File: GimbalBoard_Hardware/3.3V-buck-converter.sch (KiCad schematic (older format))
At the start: 3 parts

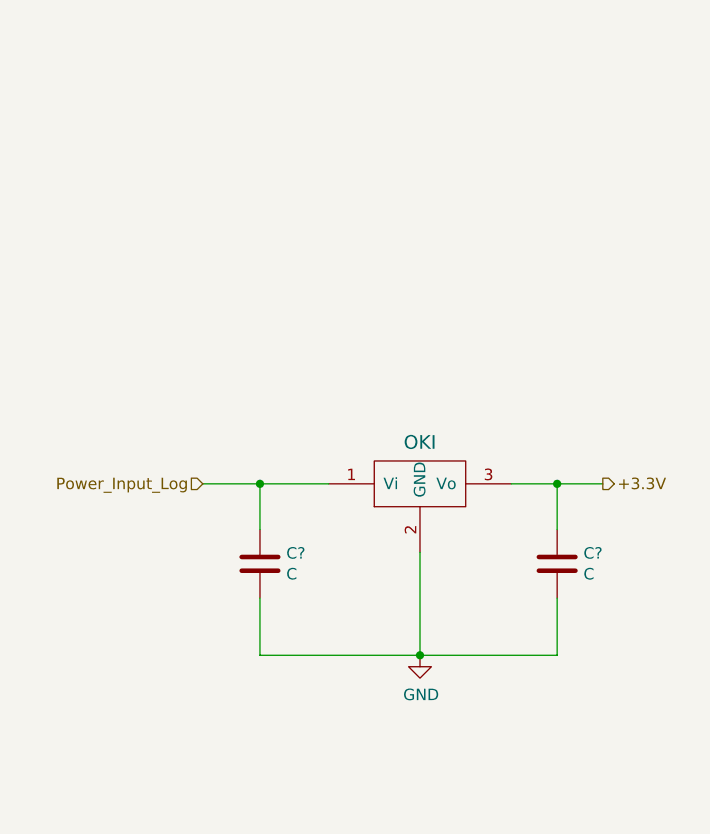
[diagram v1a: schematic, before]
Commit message: connected everything up and changed power to accomodate teensy instead of tiva
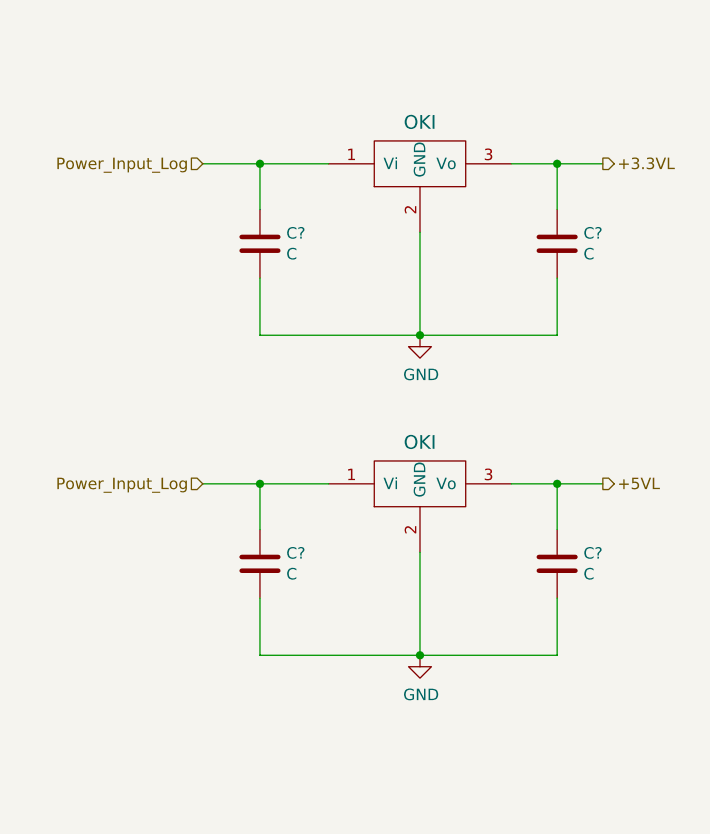
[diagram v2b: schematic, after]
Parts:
- added C? (x2): C, symbol Device:C
- added U?: OKI, symbol MRDT_Devices:OKI
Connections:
- net GND: now also C?.2, C?.2, U?.2 (GND)
- net Power_Input_Log: now also C?.1, U?.1 (Vi)
- net +3.3V renamed +5VL
- new net +3.3VL: C?.1, U?.3 (Vo)
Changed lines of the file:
@@
 $Descr A4 11693 8268
 encoding utf-8
-Sheet 2 7
+Sheet 2 8
 Title ""
 Date ""
@@
 Comment4 ""
 $EndDescr
+Wire Wire Line
+	6450 3150 6650 3150
+Wire Wire Line
+	6250 3150 6450 3150
+Connection ~ 6450 3150
+Wire Wire Line
+	6450 3350 6450 3150
+Wire Wire Line
+	5850 3900 6450 3900
+Wire Wire Line
+	5850 3450 5850 3900
+Wire Wire Line
+	6450 3650 6450 3900
+Connection ~ 5850 3900
+Wire Wire Line
+	5150 3900 5850 3900
+Wire Wire Line
+	5150 3650 5150 3900
+Wire Wire Line
+	4900 3150 5150 3150
+Wire Wire Line
+	5150 3150 5450 3150
+Connection ~ 5150 3150
+Wire Wire Line
+	5150 3150 5150 3350
 $Comp
-L Device:C C?
-U 1 1 6160C08D
-P 5150 3500
-AR Path="/6160C08D" Ref="C?"  Part="1"
-AR Path="/615B83A4/6160C08D" Ref="C?"  Part="1"
-AR Path="/6160709D/6160C08D" Ref="C?"  Part="1"
-F 0 "C?" H 5265 3546 50  0000 L CNN
-F 1 "C" H 5265 3455 50  0000 L CNN
-F 2 "" H 5188 3350 50  0001 C CNN
-F 3 "~" H 5150 3500 50  0001 C CNN
-	1    5150 3500
+L power:GND #PWR?
+U 1 1 6160C0A1
+P 5850 3900
+F 0 "#PWR?" H 5850 3650 50  0001 C CNN
+F 1 "GND" H 5855 3727 50  0000 C CNN
+F 2 "" H 5850 3900 50  0001 C CNN
+F 3 "" H 5850 3900 50  0001 C CNN
+	1    5850 3900
+	1    0    0    -1
+$EndComp
+Text HLabel 6650 3150 2    50   Output ~ 0
++5VL
+Text HLabel 4900 3150 0    50   Input ~ 0
+Power_Input_Log
+$Comp
+L MRDT_Devices:OKI U?
+U 1 1 6160C099
+P 5650 3250
+AR Path="/6160C099" Ref="U?"  Part="1"
+AR Path="/615B83A4/6160C099" Ref="U?"  Part="1"
+AR Path="/6160709D/6160C099" Ref="U?"  Part="1"
+F 0 "U?" H 5700 3200 60  0001 C CNN
+F 1 "OKI" H 5850 3531 60  0000 C CNN
+F 2 "" H 5450 3150 60  0001 C CNN
+F 3 "" H 5450 3150 60  0001 C CNN
+	1    5650 3250
 	1    0    0    -1
 $EndComp
@@
 $EndComp
 $Comp
-L MRDT_Devices:OKI U?
-U 1 1 6160C099
-P 5650 3250
-AR Path="/6160C099" Ref="U?"  Part="1"
-AR Path="/615B83A4/6160C099" Ref="U?"  Part="1"
-AR Path="/6160709D/6160C099" Ref="U?"  Part="1"
-F 0 "U?" H 5700 3200 60  0001 C CNN
-F 1 "OKI" H 5850 3531 60  0000 C CNN
-F 2 "" H 5450 3150 60  0001 C CNN
-F 3 "" H 5450 3150 60  0001 C CNN
-	1    5650 3250
-	1    0    0    -1
-$EndComp
-Text HLabel 4900 3150 0    50   Input ~ 0
-Power_Input_Log
-Text HLabel 6650 3150 2    50   Output ~ 0
-+3.3V
-$Comp
-L power:GND #PWR?
-U 1 1 6160C0A1
-P 5850 3900
-F 0 "#PWR?" H 5850 3650 50  0001 C CNN
-F 1 "GND" H 5855 3727 50  0000 C CNN
-F 2 "" H 5850 3900 50  0001 C CNN
-F 3 "" H 5850 3900 50  0001 C CNN
-	1    5850 3900
+L Device:C C?
+U 1 1 6160C08D
+P 5150 3500
+AR Path="/6160C08D" Ref="C?"  Part="1"
+AR Path="/615B83A4/6160C08D" Ref="C?"  Part="1"
+AR Path="/6160709D/6160C08D" Ref="C?"  Part="1"
+F 0 "C?" H 5265 3546 50  0000 L CNN
+F 1 "C" H 5265 3455 50  0000 L CNN
+F 2 "" H 5188 3350 50  0001 C CNN
+F 3 "~" H 5150 3500 50  0001 C CNN
+	1    5150 3500
 	1    0    0    -1
 $EndComp
 Wire Wire Line
-	5150 3150 5150 3350
+	6450 1750 6650 1750
 Wire Wire Line
-	5150 3150 5450 3150
+	6250 1750 6450 1750
+Connection ~ 6450 1750
 Wire Wire Line
-	5150 3650 5150 3900
+	6450 1950 6450 1750
 Wire Wire Line
-	5150 3900 5850 3900
+	5850 2500 6450 2500
 Wire Wire Line
-	6450 3650 6450 3900
+	5850 2050 5850 2500
 Wire Wire Line
-	5850 3450 5850 3900
-Connection ~ 5850 3900
+	6450 2250 6450 2500
+Connection ~ 5850 2500
 Wire Wire Line
-	5850 3900 6450 3900
+	5150 2500 5850 2500
 Wire Wire Line
-	6450 3350 6450 3150
+	5150 2250 5150 2500
 Wire Wire Line
-	6250 3150 6450 3150
+	4900 1750 5150 1750
 Wire Wire Line
-	4900 3150 5150 3150
-Connection ~ 5150 3150
+	5150 1750 5450 1750
+Connection ~ 5150 1750
 Wire Wire Line
-	6450 3150 6650 3150
-Connection ~ 6450 3150
+	5150 1750 5150 1950
+$Comp
+L power:GND #PWR?
+U 1 1 61623E2D
+P 5850 2500
+F 0 "#PWR?" H 5850 2250 50  0001 C CNN
+F 1 "GND" H 5855 2327 50  0000 C CNN
+F 2 "" H 5850 2500 50  0001 C CNN
+F 3 "" H 5850 2500 50  0001 C CNN
+	1    5850 2500
+	1    0    0    -1
+$EndComp
+Text HLabel 6650 1750 2    50   Output ~ 0
++3.3VL
+Text HLabel 4900 1750 0    50   Input ~ 0
+Power_Input_Log
+$Comp
+L MRDT_Devices:OKI U?
+U 1 1 61623E35
+P 5650 1850
+AR Path="/61623E35" Ref="U?"  Part="1"
+AR Path="/615B83A4/61623E35" Ref="U?"  Part="1"
+AR Path="/6160709D/61623E35" Ref="U?"  Part="1"
+F 0 "U?" H 5700 1800 60  0001 C CNN
+F 1 "OKI" H 5850 2131 60  0000 C CNN
+F 2 "" H 5450 1750 60  0001 C CNN
+F 3 "" H 5450 1750 60  0001 C CNN
+	1    5650 1850
+	1    0    0    -1
+$EndComp
+$Comp
+L Device:C C?
+U 1 1 61623E3B
+P 6450 2100
+AR Path="/61623E3B" Ref="C?"  Part="1"
+AR Path="/615B83A4/61623E3B" Ref="C?"  Part="1"
+AR Path="/6160709D/61623E3B" Ref="C?"  Part="1"
+F 0 "C?" H 6565 2146 50  0000 L CNN
+F 1 "C" H 6565 2055 50  0000 L CNN
+F 2 "" H 6488 1950 50  0001 C CNN
+F 3 "~" H 6450 2100 50  0001 C CNN
+	1    6450 2100
+	1    0    0    -1
+$EndComp
+$Comp
+L Device:C C?
+U 1 1 61623E41
+P 5150 2100
+AR Path="/61623E41" Ref="C?"  Part="1"
+AR Path="/615B83A4/61623E41" Ref="C?"  Part="1"
+AR Path="/6160709D/61623E41" Ref="C?"  Part="1"
+F 0 "C?" H 5265 2146 50  0000 L CNN
+F 1 "C" H 5265 2055 50  0000 L CNN
+F 2 "" H 5188 1950 50  0001 C CNN
+F 3 "~" H 5150 2100 50  0001 C CNN
+	1    5150 2100
+	1    0    0    -1
+$EndComp
 $EndSCHEMATC

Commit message: added h-labels
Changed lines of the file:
@@
 Wire Wire Line
 	5150 3150 5150 3350
-$Comp
-L power:GND #PWR?
-U 1 1 6160C0A1
-P 5850 3900
-F 0 "#PWR?" H 5850 3650 50  0001 C CNN
-F 1 "GND" H 5855 3727 50  0000 C CNN
-F 2 "" H 5850 3900 50  0001 C CNN
-F 3 "" H 5850 3900 50  0001 C CNN
-	1    5850 3900
-	1    0    0    -1
-$EndComp
 Text HLabel 6650 3150 2    50   Output ~ 0
 +5VL
@@
 Wire Wire Line
 	5150 1750 5150 1950
-$Comp
-L power:GND #PWR?
-U 1 1 61623E2D
-P 5850 2500
-F 0 "#PWR?" H 5850 2250 50  0001 C CNN
-F 1 "GND" H 5855 2327 50  0000 C CNN
-F 2 "" H 5850 2500 50  0001 C CNN
-F 3 "" H 5850 2500 50  0001 C CNN
-	1    5850 2500
-	1    0    0    -1
-$EndComp
 Text HLabel 6650 1750 2    50   Output ~ 0
 +3.3VL
@@
 	1    0    0    -1
 $EndComp
+Text HLabel 5850 2500 3    50   Input ~ 0
+GND
+Text HLabel 5850 3900 3    50   Input ~ 0
+GND
 $EndSCHEMATC

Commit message: added more text
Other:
- note added: "3.3VL Converter"
- note added: "5VL Converter"
- moved on the sheet: C?
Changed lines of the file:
@@
 $EndDescr
 Wire Wire Line
-	6450 3150 6650 3150
+	6450 3600 6650 3600
 Wire Wire Line
-	6250 3150 6450 3150
-Connection ~ 6450 3150
+	6250 3600 6450 3600
+Connection ~ 6450 3600
 Wire Wire Line
-	6450 3350 6450 3150
+	6450 3800 6450 3600
 Wire Wire Line
-	5850 3900 6450 3900
+	5850 4350 6450 4350
 Wire Wire Line
-	5850 3450 5850 3900
+	5850 3900 5850 4350
 Wire Wire Line
-	6450 3650 6450 3900
-Connection ~ 5850 3900
+	6450 4100 6450 4350
+Connection ~ 5850 4350
 Wire Wire Line
-	5150 3900 5850 3900
+	5150 4350 5850 4350
 Wire Wire Line
-	5150 3650 5150 3900
+	5150 4100 5150 4350
 Wire Wire Line
-	4900 3150 5150 3150
+	5150 3600 5450 3600
 Wire Wire Line
-	5150 3150 5450 3150
-Connection ~ 5150 3150
-Wire Wire Line
-	5150 3150 5150 3350
-Text HLabel 6650 3150 2    50   Output ~ 0
+	5150 3600 5150 3800
+Text HLabel 6650 3600 2    50   Output ~ 0
 +5VL
-Text HLabel 4900 3150 0    50   Input ~ 0
-Power_Input_Log
 $Comp
 L MRDT_Devices:OKI U?
 U 1 1 6160C099
-P 5650 3250
+P 5650 3700
 AR Path="/6160C099" Ref="U?"  Part="1"
 AR Path="/615B83A4/6160C099" Ref="U?"  Part="1"
 AR Path="/6160709D/6160C099" Ref="U?"  Part="1"
-F 0 "U?" H 5700 3200 60  0001 C CNN
-F 1 "OKI" H 5850 3531 60  0000 C CNN
-F 2 "" H 5450 3150 60  0001 C CNN
-F 3 "" H 5450 3150 60  0001 C CNN
-	1    5650 3250
+F 0 "U?" H 5700 3650 60  0001 C CNN
+F 1 "OKI" H 5850 3981 60  0000 C CNN
+F 2 "" H 5450 3600 60  0001 C CNN
+F 3 "" H 5450 3600 60  0001 C CNN
+	1    5650 3700
 	1    0    0    -1
 $EndComp
@@
 L Device:C C?
 U 1 1 6160C093
-P 6450 3500
+P 6450 3950
 AR Path="/6160C093" Ref="C?"  Part="1"
 AR Path="/615B83A4/6160C093" Ref="C?"  Part="1"
 AR Path="/6160709D/6160C093" Ref="C?"  Part="1"
-F 0 "C?" H 6565 3546 50  0000 L CNN
-F 1 "C" H 6565 3455 50  0000 L CNN
-F 2 "" H 6488 3350 50  0001 C CNN
-F 3 "~" H 6450 3500 50  0001 C CNN
-	1    6450 3500
+F 0 "C?" H 6565 3996 50  0000 L CNN
+F 1 "C" H 6565 3905 50  0000 L CNN
+F 2 "" H 6488 3800 50  0001 C CNN
+F 3 "~" H 6450 3950 50  0001 C CNN
+	1    6450 3950
 	1    0    0    -1
 $EndComp
@@
 L Device:C C?
 U 1 1 6160C08D
-P 5150 3500
+P 5150 3950
 AR Path="/6160C08D" Ref="C?"  Part="1"
 AR Path="/615B83A4/6160C08D" Ref="C?"  Part="1"
 AR Path="/6160709D/6160C08D" Ref="C?"  Part="1"
-F 0 "C?" H 5265 3546 50  0000 L CNN
-F 1 "C" H 5265 3455 50  0000 L CNN
-F 2 "" H 5188 3350 50  0001 C CNN
-F 3 "~" H 5150 3500 50  0001 C CNN
-	1    5150 3500
+F 0 "C?" H 5265 3996 50  0000 L CNN
+F 1 "C" H 5265 3905 50  0000 L CNN
+F 2 "" H 5188 3800 50  0001 C CNN
+F 3 "~" H 5150 3950 50  0001 C CNN
+	1    5150 3950
 	1    0    0    -1
 $EndComp
@@
 	5150 2250 5150 2500
 Wire Wire Line
-	4900 1750 5150 1750
-Wire Wire Line
 	5150 1750 5450 1750
 Connection ~ 5150 1750
@@
 Text HLabel 6650 1750 2    50   Output ~ 0
 +3.3VL
-Text HLabel 4900 1750 0    50   Input ~ 0
-Power_Input_Log
 $Comp
 L MRDT_Devices:OKI U?
@@
 Text HLabel 5850 2500 3    50   Input ~ 0
 GND
-Text HLabel 5850 3900 3    50   Input ~ 0
+Text HLabel 5850 4350 3    50   Input ~ 0
 GND
+Wire Wire Line
+	4900 1750 5150 1750
+Text HLabel 4900 1750 0    50   Input ~ 0
+Power_Input_Log
+Connection ~ 5150 3600
+Text HLabel 4900 3600 0    50   Input ~ 0
+Power_Input_Log
+Wire Wire Line
+	4900 3600 5150 3600
+Text Notes 5350 1300 0    79   ~ 0
+3.3VL Converter
+Text Notes 5500 3200 0    79   ~ 0
+5VL Converter
 $EndSCHEMATC

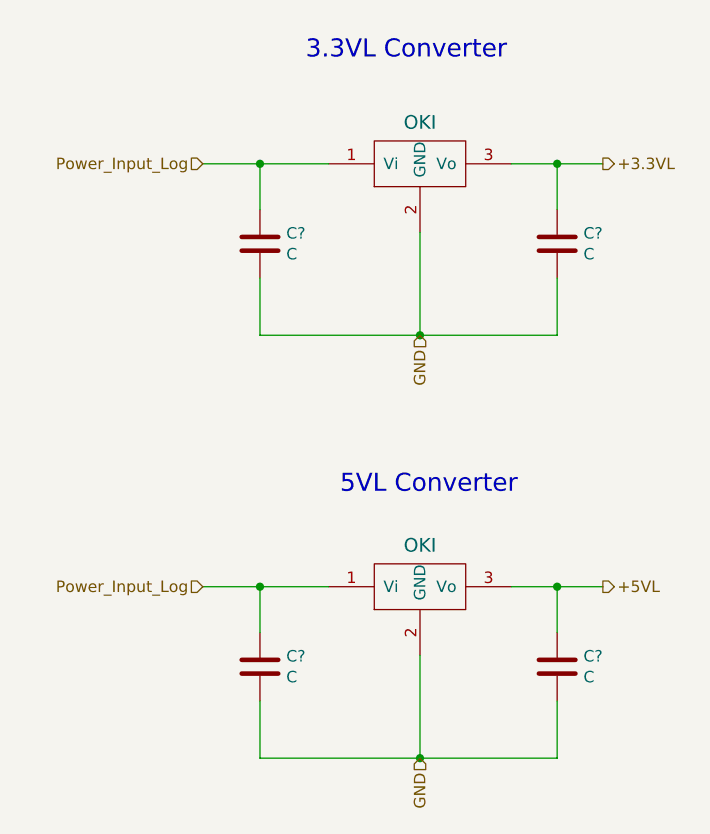
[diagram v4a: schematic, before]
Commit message: added labels, numbered everything, added no connection to pins. Still can't get past a couple pf errors in the electrical rules check
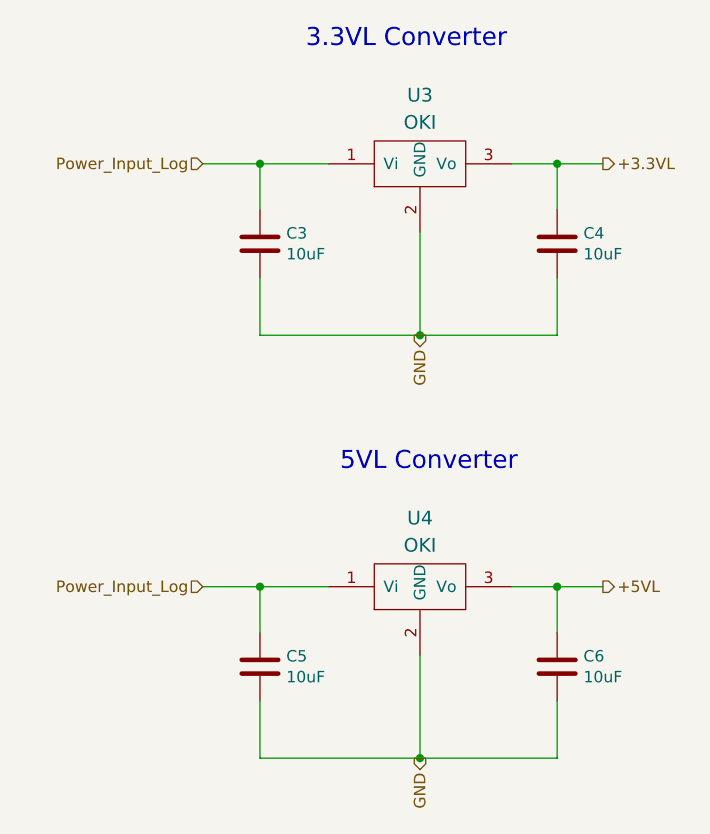
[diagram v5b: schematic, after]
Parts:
- C3, C4, C5, C6: renamed from C?; value C -> 10uF
- gave numbers to parts that had none: 2
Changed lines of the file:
@@
 AR Path="/6160C099" Ref="U?"  Part="1"
 AR Path="/615B83A4/6160C099" Ref="U?"  Part="1"
-AR Path="/6160709D/6160C099" Ref="U?"  Part="1"
-F 0 "U?" H 5700 3650 60  0001 C CNN
+AR Path="/6160709D/6160C099" Ref="U4"  Part="1"
+F 0 "U4" H 5850 4100 60  0000 C CNN
 F 1 "OKI" H 5850 3981 60  0000 C CNN
 F 2 "" H 5450 3600 60  0001 C CNN
@@
 AR Path="/6160C093" Ref="C?"  Part="1"
 AR Path="/615B83A4/6160C093" Ref="C?"  Part="1"
-AR Path="/6160709D/6160C093" Ref="C?"  Part="1"
-F 0 "C?" H 6565 3996 50  0000 L CNN
-F 1 "C" H 6565 3905 50  0000 L CNN
+AR Path="/6160709D/6160C093" Ref="C6"  Part="1"
+F 0 "C6" H 6565 3996 50  0000 L CNN
+F 1 "10uF" H 6565 3905 50  0000 L CNN
 F 2 "" H 6488 3800 50  0001 C CNN
 F 3 "~" H 6450 3950 50  0001 C CNN
@@
 AR Path="/6160C08D" Ref="C?"  Part="1"
 AR Path="/615B83A4/6160C08D" Ref="C?"  Part="1"
-AR Path="/6160709D/6160C08D" Ref="C?"  Part="1"
-F 0 "C?" H 5265 3996 50  0000 L CNN
-F 1 "C" H 5265 3905 50  0000 L CNN
+AR Path="/6160709D/6160C08D" Ref="C5"  Part="1"
+F 0 "C5" H 5265 3996 50  0000 L CNN
+F 1 "10uF" H 5265 3905 50  0000 L CNN
 F 2 "" H 5188 3800 50  0001 C CNN
 F 3 "~" H 5150 3950 50  0001 C CNN
@@
 AR Path="/61623E35" Ref="U?"  Part="1"
 AR Path="/615B83A4/61623E35" Ref="U?"  Part="1"
-AR Path="/6160709D/61623E35" Ref="U?"  Part="1"
-F 0 "U?" H 5700 1800 60  0001 C CNN
+AR Path="/6160709D/61623E35" Ref="U3"  Part="1"
+F 0 "U3" H 5850 2250 60  0000 C CNN
 F 1 "OKI" H 5850 2131 60  0000 C CNN
 F 2 "" H 5450 1750 60  0001 C CNN
@@
 AR Path="/61623E3B" Ref="C?"  Part="1"
 AR Path="/615B83A4/61623E3B" Ref="C?"  Part="1"
-AR Path="/6160709D/61623E3B" Ref="C?"  Part="1"
-F 0 "C?" H 6565 2146 50  0000 L CNN
-F 1 "C" H 6565 2055 50  0000 L CNN
+AR Path="/6160709D/61623E3B" Ref="C4"  Part="1"
+F 0 "C4" H 6565 2146 50  0000 L CNN
+F 1 "10uF" H 6565 2055 50  0000 L CNN
 F 2 "" H 6488 1950 50  0001 C CNN
 F 3 "~" H 6450 2100 50  0001 C CNN
@@
 AR Path="/61623E41" Ref="C?"  Part="1"
 AR Path="/615B83A4/61623E41" Ref="C?"  Part="1"
-AR Path="/6160709D/61623E41" Ref="C?"  Part="1"
-F 0 "C?" H 5265 2146 50  0000 L CNN
-F 1 "C" H 5265 2055 50  0000 L CNN
+AR Path="/6160709D/61623E41" Ref="C3"  Part="1"
+F 0 "C3" H 5265 2146 50  0000 L CNN
+F 1 "10uF" H 5265 2055 50  0000 L CNN
 F 2 "" H 5188 1950 50  0001 C CNN
 F 3 "~" H 5150 2100 50  0001 C CNN
@@
 	1    0    0    -1
 $EndComp
-Text HLabel 5850 2500 3    50   Input ~ 0
+Text HLabel 5850 2500 3    50   Output ~ 0
 GND
-Text HLabel 5850 4350 3    50   Input ~ 0
+Text HLabel 5850 4350 3    50   Output ~ 0
 GND
 Wire Wire Line
@@
 Wire Wire Line
 	4900 3600 5150 3600
-Text Notes 5350 1300 0    79   ~ 0
+Text Notes 5350 1250 0    79   ~ 0
 3.3VL Converter
-Text Notes 5500 3200 0    79   ~ 0
+Text Notes 5500 3100 0    79   ~ 0
 5VL Converter
 $EndSCHEMATC
